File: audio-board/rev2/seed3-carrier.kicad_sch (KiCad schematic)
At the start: 56 parts, among them J1 AudioJack2_Switch, J2 AudioJack2, J3 POWER_BOARD, J4 DISPLAY_UART, J5 SJ3-35063AG, J8 LINE_OUT, J9 SJ3-35063AG, Q1 AO3401A, Q4 2N7002, U1 TLV9064IDR, U2 TPA6132A2RTE

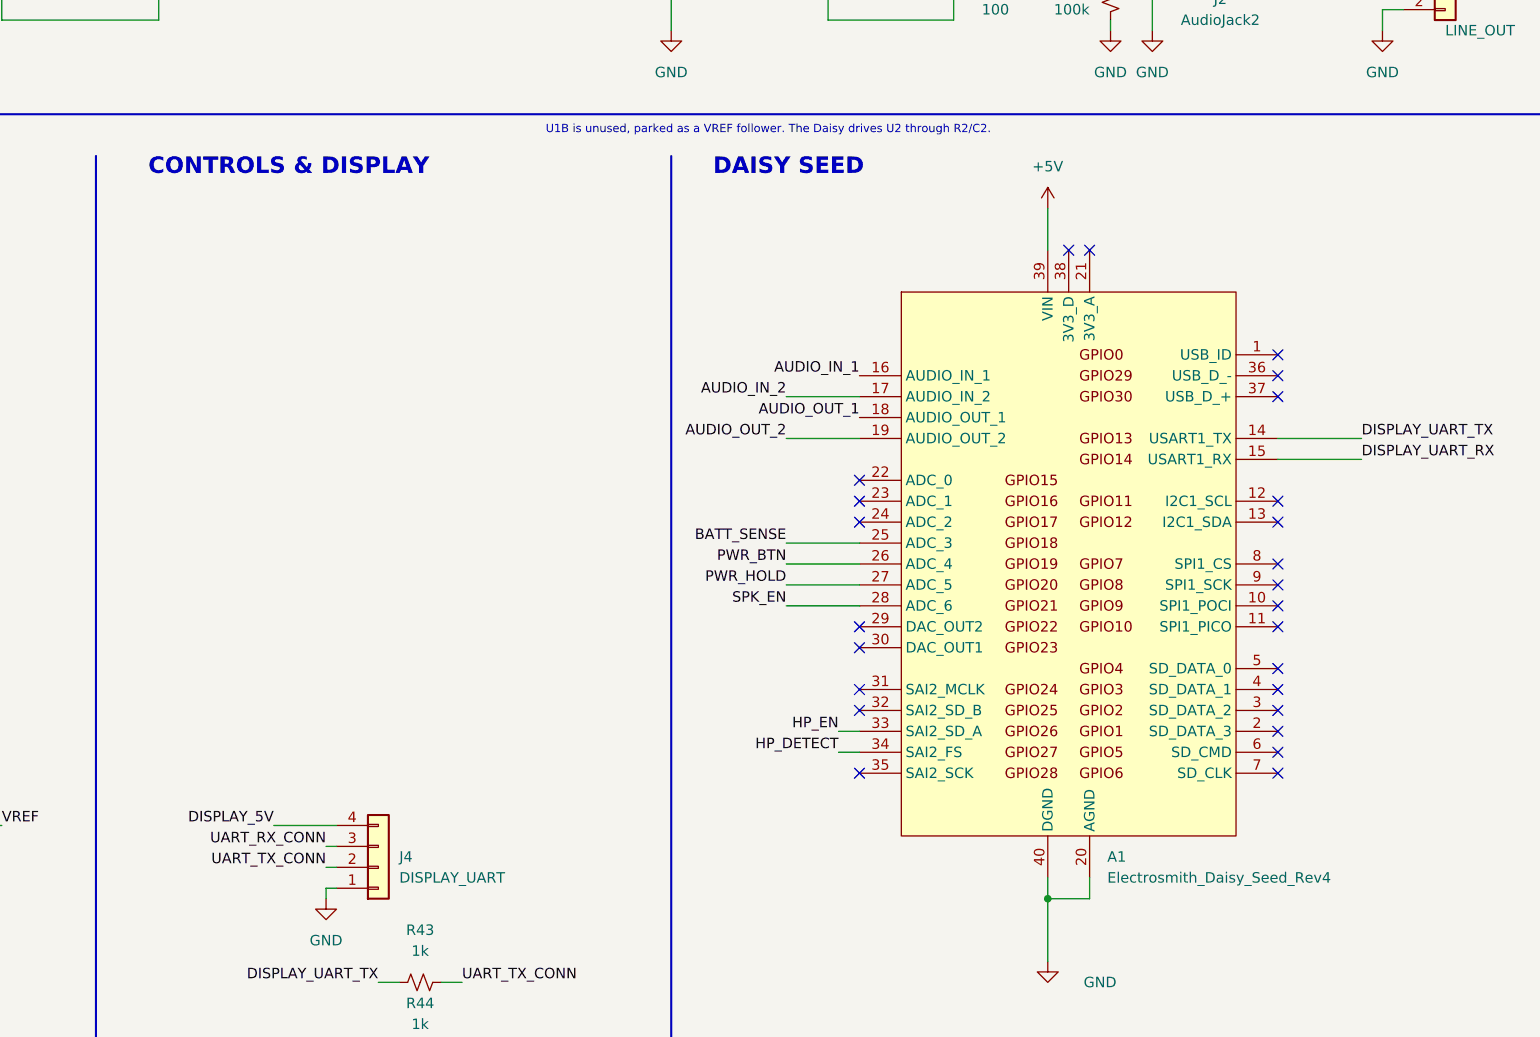
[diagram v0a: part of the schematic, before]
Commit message: Fix stale heading, A1 value and 3D models
- Rename the schematic's CONTROLS & DISPLAY heading to DISPLAY; the
  encoder it covered is gone.
- A1's value is now "Daisy Seed3" instead of the Rev 4 symbol name, so
  the BOM names the right module.
- A1, J1 and J2 pointed at KiCad 3D models that don't exist. A1 now
  uses the repo's Daisy placeholder on two 8.5 mm 1x20 socket models,
  and J1/J2 use the Neutrik placeholder.
- Remove the unused PTV09A pot footprint and the pot and SJ1-3535NG
  placeholders, along with their code in make_placeholders.py.

Co-Authored-By: Claude Opus 5.5 <noreply@anthropic.com>
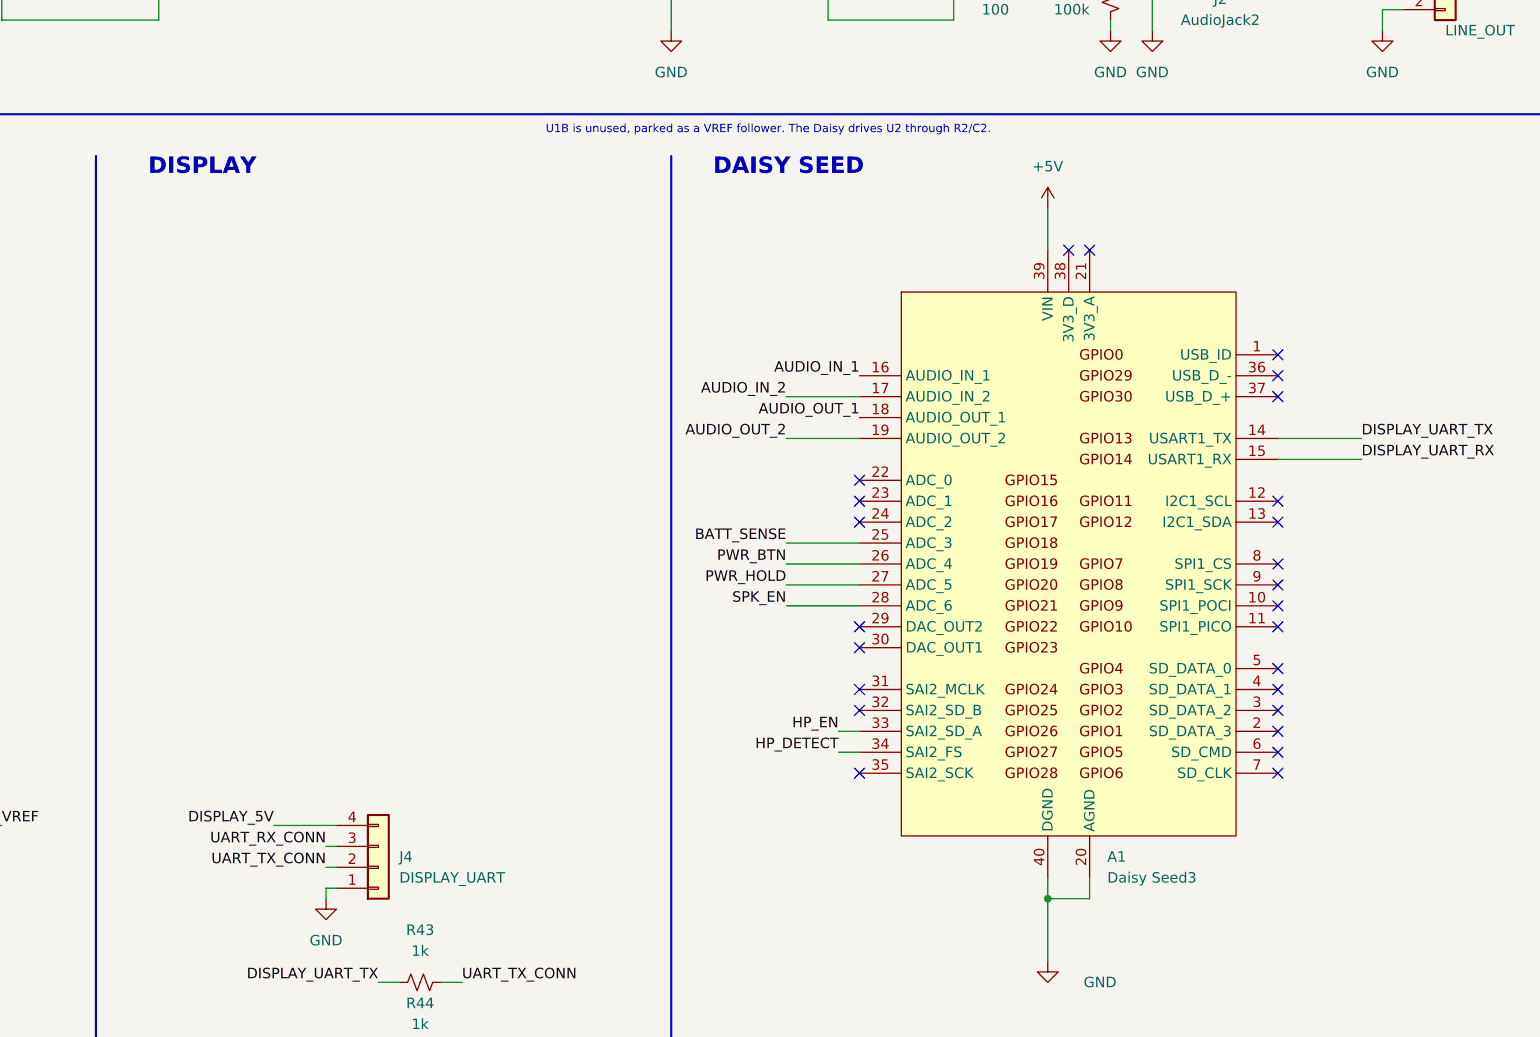
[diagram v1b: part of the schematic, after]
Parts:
- A1: value Electrosmith_Daisy_Seed_Rev4 -> Daisy Seed3
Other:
- note added: "DISPLAY"
- note removed: "CONTROLS & DISPLAY"
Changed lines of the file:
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@@
 		)
 	)
-	(text "CONTROLS & DISPLAY"
+	(text "DISPLAY"
 		(exclude_from_sim no)
 		(at 106.68 71.12 0)
@@
 			)
 		)
-		(property "Value" "Electrosmith_Daisy_Seed_Rev4"
+		(property "Value" "Daisy Seed3"
 			(at 223.1233 156.21 0)
 			(show_name no)

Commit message: Isolate HP_EN from U2 and fix the AUX and line-out levels
The Daisy can run from USB while the carrier's +5V is off. HP_EN then
drove U2's EN pin above its VDD + 0.3 V rating. U4 (TXU0101) now sits
between HP_EN and EN, powered from the Daisy's 3V3_D and +5V. Its
output goes high-impedance when either supply is off, and R26 holds
EN low.

- R38 47k -> 4.7k: with the same signal on both AUX channels, 2 Vrms
  reached the Daisy at 4.9 Vpp, over its 3.6 Vpp range. Now 2.7 Vpp.
- R43 1k -> 10k: limits current into an unpowered display. Caps the
  display UART at 230400 baud.
- Speaker enable delay raised from 0.5 s to 4 s after power-on, so the
  line-out bias settles before the speaker amp unmutes.
- DESIGN.md, CHANGES.md and TEST_PLAN.md updated to match.

Co-Authored-By: Claude Opus 5.5 <noreply@anthropic.com>
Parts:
- added C37, C38: 100nF, Capacitor_SMD:C_1206_3216Metric_Pad1.33x1.80mm_HandSolder, symbol Device:C_Small
- added U4: TXU0101, Package_TO_SOT_SMD:SOT-23-6, symbol seed3-carrier:TXU0101DBV
- R38: value 47k -> 4.7k; LCSC C25833 -> C17936
- R43: value 1k -> 10k; LCSC C4410 -> C17902
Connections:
- net +5V: now also C38.1, U4.6 (V_{CCB})
- net GND: now also C37.2, C38.2, U4.2 (GND)
- net HP_EN: now also U4.3 (A); no longer R26.1, U2.13 (EN)
- net 3V3_D: now reaches A1.38 (3V3_D)
- net 3V3_D: now also C37.1, U4.1 (V_{CCA}), U4.5 (OE)
- new net U2_EN: R26.1, U2.13 (EN), U4.4 (BY)
- no-connect marks 28 -> 27
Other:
- note added: "HP_EN (Daisy pin 33) drives U2 EN through U4 (TXU0101, 3V3_D to +5V). U4 has a pull-down on A and goes Hi-Z when either supply is off, and R26 holds U2_EN low, so U2 stays off while the Daisy is absent, booting, in DFU, being reset, or running from USB with +5V off. The firmware feeds the STM32 internal watchdog (IWDG) only from the audio callback: if audio stops, the STM32 resets, its pins float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"
- note added: "U2: TPA6132A2 DirectPath, gain 0 dB (G0 high, G1 low). Outputs sit at 0 V: no output caps. C12/C13 with the 19.8k internal input R: 1.7 Hz high-pass. EN = U2_EN from U4, pulled low by R26. Layout: run SGND straight to the J5 sleeve pin. HPVDD/HPVSS are made inside U2: caps only."
- note removed: "HP_EN (Daisy pin 33) drives U2 EN directly. R26 holds it low, so U2 stays off while the Daisy is absent, booting, in DFU or being reset. The firmware feeds the STM32 internal watchdog (IWDG) only from the audio callback: if audio stops, the STM32 resets, its pins float, and R26 (U2) and R37 (Q4, speaker) mute both amps. The speaker amp mute is SPK_MUTE on J3."
- note removed: "U2: TPA6132A2 DirectPath, gain 0 dB (G0 high, G1 low). Outputs sit at 0 V: no output caps. C12/C13 with the 19.8k internal input R: 1.7 Hz high-pass. EN = HP_EN, pulled low by R26. Layout: run SGND straight to the J5 sleeve pin. HPVDD/HPVSS are made inside U2: caps only."

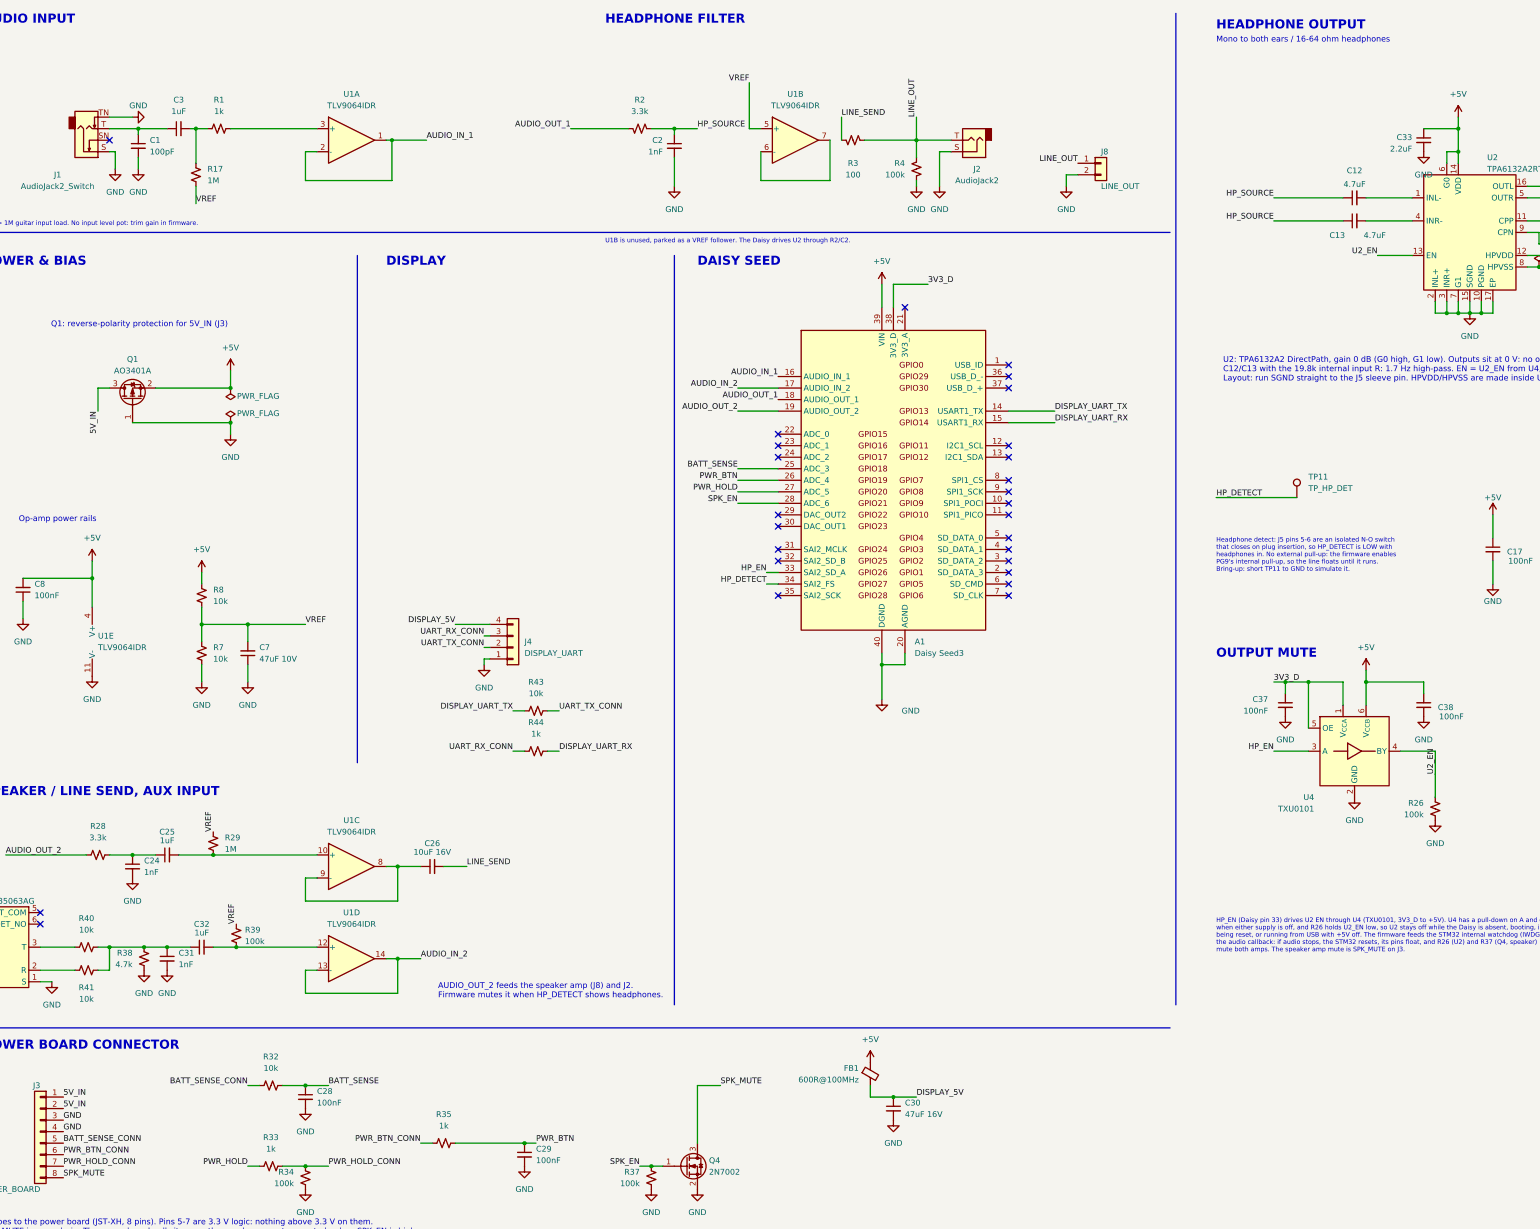
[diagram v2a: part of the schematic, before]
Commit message: Remove the line-out buffer and return U1 to a TLV9062
The Seed3's outputs are AC-coupled and can drive a cable directly, so
R28/C24 now feed LINE_OUT without U1C, C25, R29, C26 or R3. That also
removes the power-on drift and the 4 s speaker-enable delay. With U1C
and the parked unit gone, U1 is a TLV9062 dual and the AUX buffer is
U1B. J2 stays live with headphones in, for recording while monitoring.

Co-Authored-By: Claude Opus 5.5 <noreply@anthropic.com>
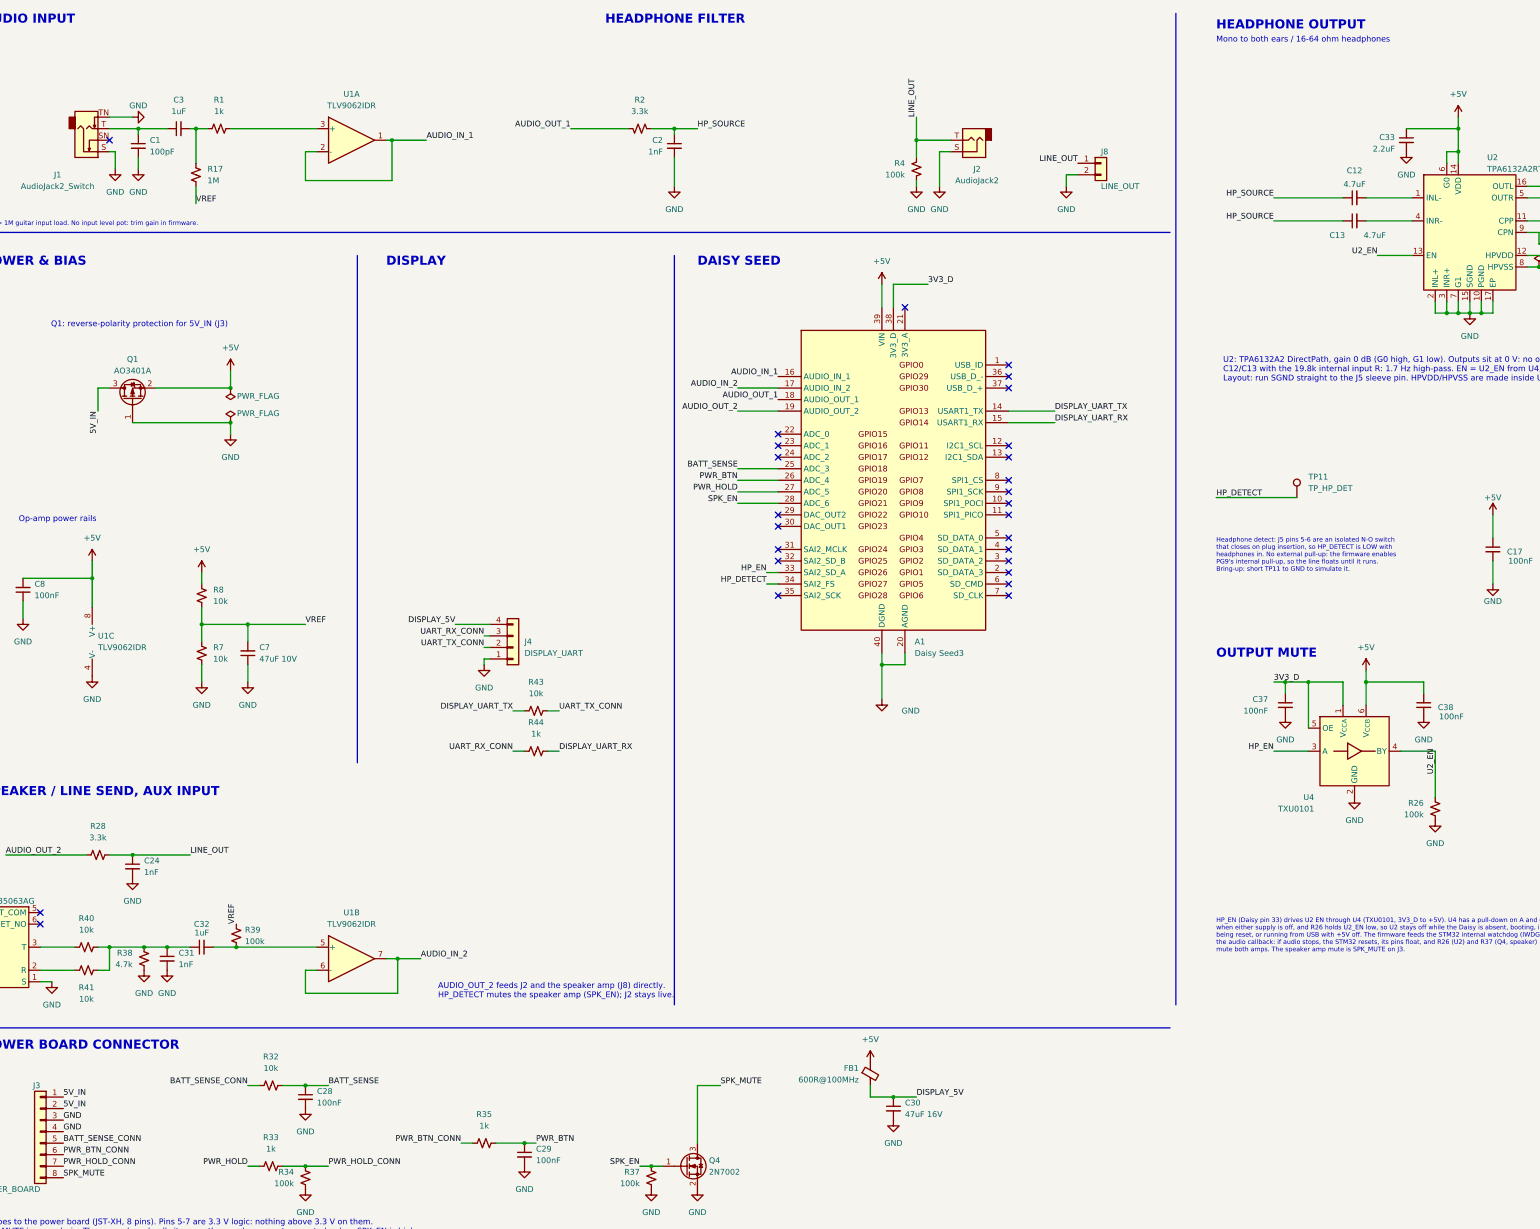
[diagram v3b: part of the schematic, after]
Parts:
- removed C25: 1uF, Capacitor_SMD:C_1206_3216Metric_Pad1.33x1.80mm_HandSolder, symbol Device:C_Small
- removed C26: 10uF 16V, Capacitor_SMD:C_1206_3216Metric_Pad1.33x1.80mm_HandSolder, symbol Device:C_Small
- removed R29: 1M, Resistor_SMD:R_1206_3216Metric_Pad1.30x1.75mm_HandSolder, symbol Device:R_Small_US
- removed R3: 100, Resistor_SMD:R_1206_3216Metric_Pad1.30x1.75mm_HandSolder, symbol Device:R_Small_US
- removed unit 2 of U1
- removed unit 3 of U1
- U1: value TLV9064IDR -> TLV9062IDR; footprint Package_SO:SOIC-14_3.9x8.7mm_P1.27mm -> Package_SO:SOIC-8_3.9x4.9mm_P1.27mm; symbol Amplifier_Operational:TL074 -> Amplifier_Operational:TL072; LCSC C388176 -> C398355
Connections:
- net +5V: now also U1.8 (V+); no longer U1.4 (V+)
- net AUDIO_IN_2: now also U1.6 (-), U1.7; no longer U1.13 (-), U1.14
- net GND: now also U1.4 (V-); no longer U1.11 (V-)
- net LINE_OUT: now also C24.1, R28.2
- net at C32.2, R39.2: now also U1.5 (+); no longer U1.12 (+)
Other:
- note added: "AUDIO_OUT_2 feeds J2 and the speaker amp (J8) directly. HP_DETECT mutes the speaker amp (SPK_EN); J2 stays live."
- note removed: "AUDIO_OUT_2 feeds the speaker amp (J8) and J2. Firmware mutes it when HP_DETECT shows headphones."
- note removed: "U1B is unused, parked as a VREF follower. The Daisy drives U2 through R2/C2."
- moved on the sheet: C33, R35
